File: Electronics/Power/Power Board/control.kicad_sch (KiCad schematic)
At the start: 45 parts, among them IC1 STM32U575VGT6, IC302 TJA1057GT/3, J1 TYPE-C-31-M-12, J304 Pluggable_Terminal_01x03, J304 TC2030, SW301 SW_DIP_x02, U1 USBLC6-4SC6-ES, U2 USBLC6-4SC6-ES, U303 TVS1800DRV, X301 25MHz_Clock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

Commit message: Sensor hub board done
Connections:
- net CC1: now also U1.3 (IO2); no longer U1.1 (IO1)
- net CC2: now also U1.1 (IO1); no longer U1.3 (IO2)
- net USB_DN: now also U1.4 (IO3); no longer U1.6 (IO4)
- net USB_DP: now also U1.6 (IO4); no longer U1.4 (IO3)
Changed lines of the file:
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@@
   (junction (at 34.29 224.79) (diameter 0) (color 0 0 0 0)
   )
-  (junction (at 345.44 105.41) (diameter 0) (color 0 0 0 0)
-  )
   (junction (at 132.08 257.81) (diameter 0) (color 0 0 0 0)
   )
@@
   (junction (at 34.29 201.93) (diameter 0) (color 0 0 0 0)
   )
-  (junction (at 342.9 107.95) (diameter 0) (color 0 0 0 0)
+  (junction (at 345.44 107.95) (diameter 0) (color 0 0 0 0)
   )
   (junction (at 330.2 161.29) (diameter 0) (color 0 0 0 0)
@@
   (junction (at 320.04 161.29) (diameter 0) (color 0 0 0 0)
   )
+  (junction (at 342.9 105.41) (diameter 0) (color 0 0 0 0)
+  )
   (junction (at 360.68 171.45) (diameter 0) (color 0 0 0 0)
   )
@@
     (stroke (width 0) (type default))
   )
-  (wire (pts (xy 335.28 107.95) (xy 342.9 107.95))
-    (stroke (width 0) (type default))
-  )
   (wire (pts (xy 81.28 259.08) (xy 78.74 259.08))
     (stroke (width 0) (type default))
@@
     (stroke (width 0) (type default))
   )
+  (wire (pts (xy 337.82 113.03) (xy 337.82 97.79))
+    (stroke (width 0) (type default))
+  )
   (wire (pts (xy 359.41 53.34) (xy 359.41 55.88))
     (stroke (width 0) (type default))
@@
     (stroke (width 0) (type default))
   )
+  (wire (pts (xy 345.44 107.95) (xy 351.79 107.95))
+    (stroke (width 0) (type default))
+  )
   (polyline (pts (xy 377.19 204.47) (xy 377.19 243.84))
     (stroke (width 0) (type default))
@@
     (stroke (width 0) (type default))
   )
-  (wire (pts (xy 337.82 95.25) (xy 354.33 95.25))
-    (stroke (width 0) (type default))
-  )
   (wire (pts (xy 157.48 134.62) (xy 157.48 132.08))
     (stroke (width 0) (type default))
@@
     (stroke (width 0) (type default))
   )
-  (wire (pts (xy 342.9 107.95) (xy 351.79 107.95))
+  (wire (pts (xy 335.28 107.95) (xy 345.44 107.95))
     (stroke (width 0) (type default))
   )
@@
     (stroke (width 0) (type default))
   )
+  (wire (pts (xy 345.44 107.95) (xy 345.44 113.03))
+    (stroke (width 0) (type default))
+  )
   (wire (pts (xy 344.17 214.63) (xy 344.17 217.17))
     (stroke (width 0) (type default))
@@
     (stroke (width 0) (type default))
   )
-  (wire (pts (xy 49.53 215.9) (xy 59.69 215.9))
+  (wire (pts (xy 342.9 105.41) (xy 351.79 105.41))
     (stroke (width 0) (type default))
   )
-  (wire (pts (xy 342.9 107.95) (xy 342.9 113.03))
+  (wire (pts (xy 49.53 215.9) (xy 59.69 215.9))
     (stroke (width 0) (type default))
   )
@@
     (stroke (width 0) (type default))
   )
+  (wire (pts (xy 340.36 95.25) (xy 354.33 95.25))
+    (stroke (width 0) (type default))
+  )
   (wire (pts (xy 35.56 146.05) (xy 40.64 146.05))
     (stroke (width 0) (type default))
@@
     (stroke (width 0) (type default))
   )
-  (wire (pts (xy 345.44 105.41) (xy 351.79 105.41))
+  (wire (pts (xy 335.28 105.41) (xy 342.9 105.41))
     (stroke (width 0) (type default))
   )
@@
     (stroke (width 0) (type default))
   )
-  (wire (pts (xy 335.28 105.41) (xy 345.44 105.41))
-    (stroke (width 0) (type default))
-  )
   (wire (pts (xy 228.6 60.96) (xy 228.6 63.5))
     (stroke (width 0) (type default))
@@
     (stroke (width 0) (type default))
   )
+  (wire (pts (xy 340.36 95.25) (xy 340.36 113.03))
+    (stroke (width 0) (type default))
+  )
   (wire (pts (xy 60.96 166.37) (xy 60.96 163.83))
     (stroke (width 0) (type default))
@@
     (stroke (width 0) (type default))
   )
-  (wire (pts (xy 340.36 97.79) (xy 354.33 97.79))
+  (wire (pts (xy 337.82 97.79) (xy 354.33 97.79))
     (stroke (width 0) (type default))
   )
@@
     (stroke (width 0) (type default))
   )
-  (wire (pts (xy 340.36 97.79) (xy 340.36 113.03))
-    (stroke (width 0) (type default))
-  )
   (wire (pts (xy 356.87 48.26) (xy 374.65 48.26))
     (stroke (width 0) (type default))
@@
     (stroke (width 0) (type default))
   )
-  (wire (pts (xy 337.82 95.25) (xy 337.82 113.03))
-    (stroke (width 0) (type default))
-  )
   (wire (pts (xy 34.29 223.52) (xy 34.29 224.79))
     (stroke (width 0) (type default))
@@
     (stroke (width 0) (type default))
   )
-  (wire (pts (xy 129.54 270.51) (xy 140.97 270.51))
+  (wire (pts (xy 342.9 105.41) (xy 342.9 113.03))
     (stroke (width 0) (type default))
   )
-  (wire (pts (xy 345.44 105.41) (xy 345.44 113.03))
+  (wire (pts (xy 129.54 270.51) (xy 140.97 270.51))
     (stroke (width 0) (type default))
   )
@@
     )
   )
+  (netclass_flag "" (length 2.54) (shape round) (at 242.57 96.52 0) (fields_autoplaced)
+    (effects (font (size 1.27 1.27)) (justify left bottom))
+    (property "Netclass" "USB" (at 243.2685 93.98 0)
+      (effects (font (size 1.27 1.27) italic) (justify left))
+    )
+  )
+  (netclass_flag "" (length 2.54) (shape round) (at 242.57 99.06 0) (fields_autoplaced)
+    (effects (font (size 1.27 1.27)) (justify left bottom))
+    (property "Netclass" "USB" (at 243.2685 96.52 0)
+      (effects (font (size 1.27 1.27) italic) (justify left))
+    )
+  )
   (symbol (lib_id "Device:R_Small") (at 63.5 97.79 180) (unit 1)
     (in_bom yes) (on_board yes) (dnp no)
@@
     )
   )
-  (symbol (lib_name "USBLC6-4SC6-ES_1") (lib_id "MSL_Symbols:USBLC6-4SC6-ES") (at 342.9 120.65 0) (unit 1)
+  (symbol (lib_id "MSL_Symbols:USBLC6-4SC6-ES") (at 342.9 120.65 0) (unit 1)
     (in_bom yes) (on_board yes) (dnp no) (fields_autoplaced)
     (property "Reference" "U1" (at 351.79 119.38 0)
@@
       (effects (font (size 1.27 1.27)) hide)
     )
-    (property "Datasheet" "" (at 52.07 228.6 0)
+    (property "Datasheet" "https://datasheet.lcsc.com/lcsc/2209201730_ElecSuper-USBLC6-4SC6-ES_C5180279.pdf" (at 52.07 228.6 0)
       (effects (font (size 1.27 1.27)) hide)
     )

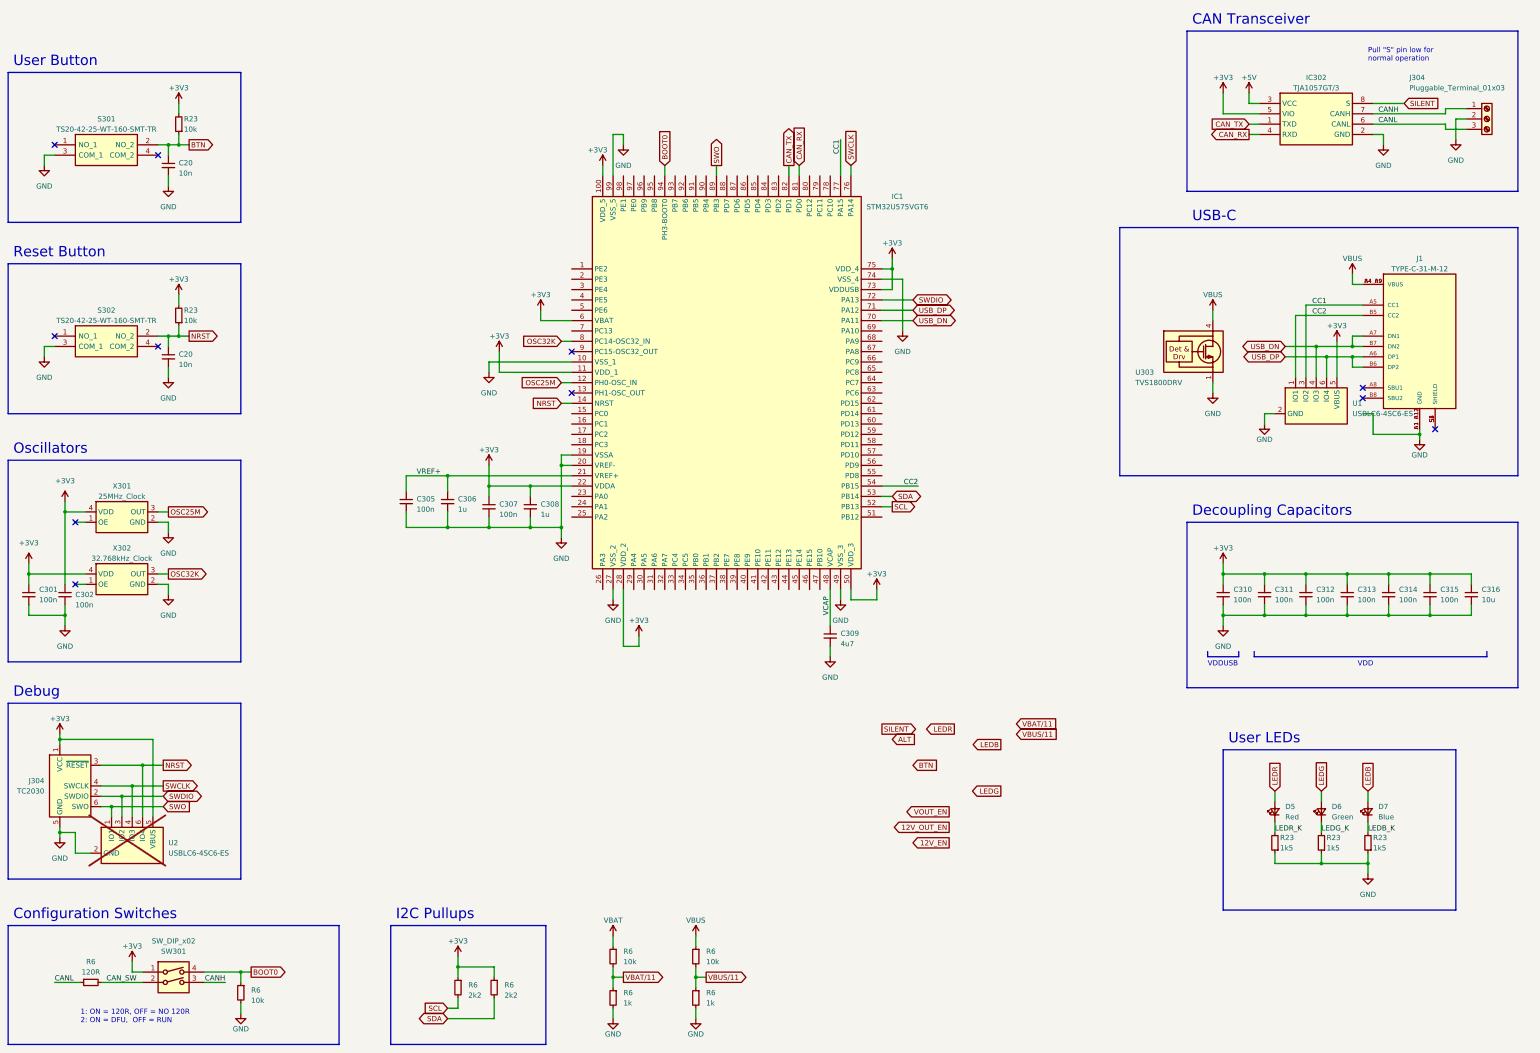
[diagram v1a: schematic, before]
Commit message: Motor driver and power boards done
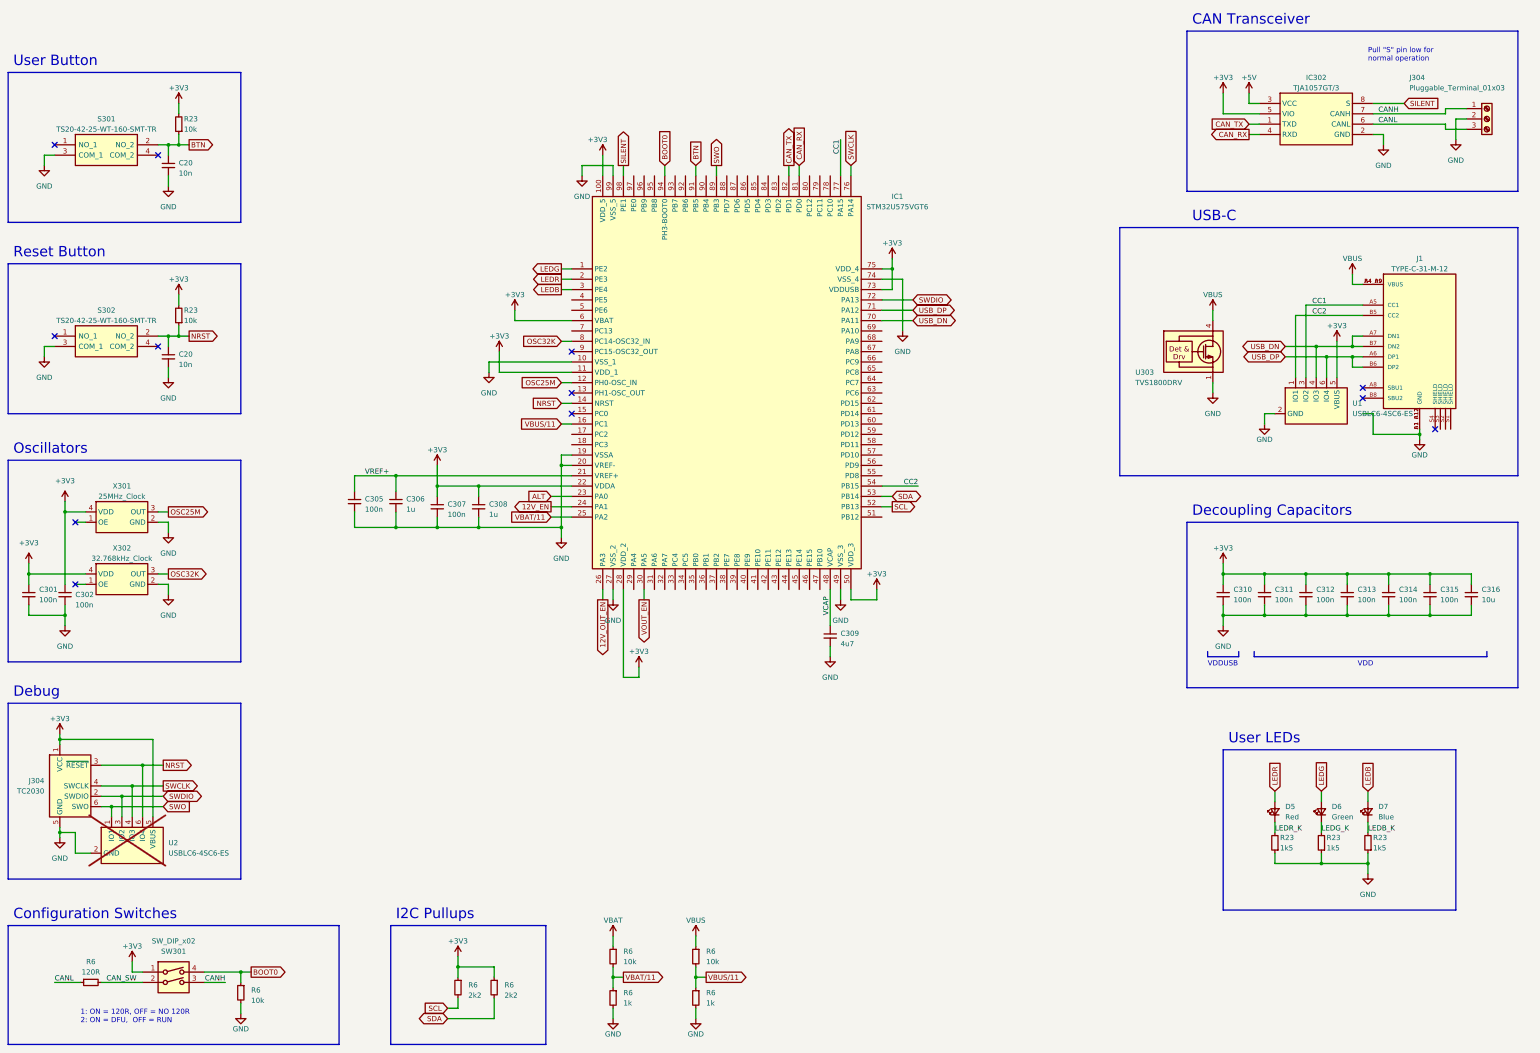
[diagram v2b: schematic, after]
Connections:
- net 12V_EN: now also IC1.24 (PA1)
- net 12V_OUT_EN: now also IC1.26 (PA3)
- net ALT: now also IC1.23 (PA0)
- net BTN: now also IC1.91 (PB5)
- net LEDB: now also IC1.3 (PE4)
- net LEDG: now also IC1.1 (PE2)
- net LEDR: now also IC1.2 (PE3)
- net SILENT: now also IC1.98 (PE1)
- net VBAT/11: now also IC1.25 (PA2)
- net VBUS/11: now also IC1.16 (PC1)
- net VOUT_EN: now also IC1.30 (PA5)
- now unconnected: J1.S1 (SHIELD), J1.S2 (SHIELD), J1.S3 (SHIELD), J1.S4 (SHIELD)
- no-connect marks 11 -> 12
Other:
- moved on the sheet: C305, C306, C307, C308
